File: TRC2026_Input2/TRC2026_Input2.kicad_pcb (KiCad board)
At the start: 2 copper layers, 144 x 63.3 mm, 26 parts, among them J1 ジョイスティック, J2 Conn_01x06_Pin, J3 Conn_01x05_Pin, J4 1F接続, J5 Conn_01x05_Pin, J6 Conn_01x05_Pin, SW1 SW_Push, SW2 SW_Push, SW3 SW_Push, SW4 SW_Push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

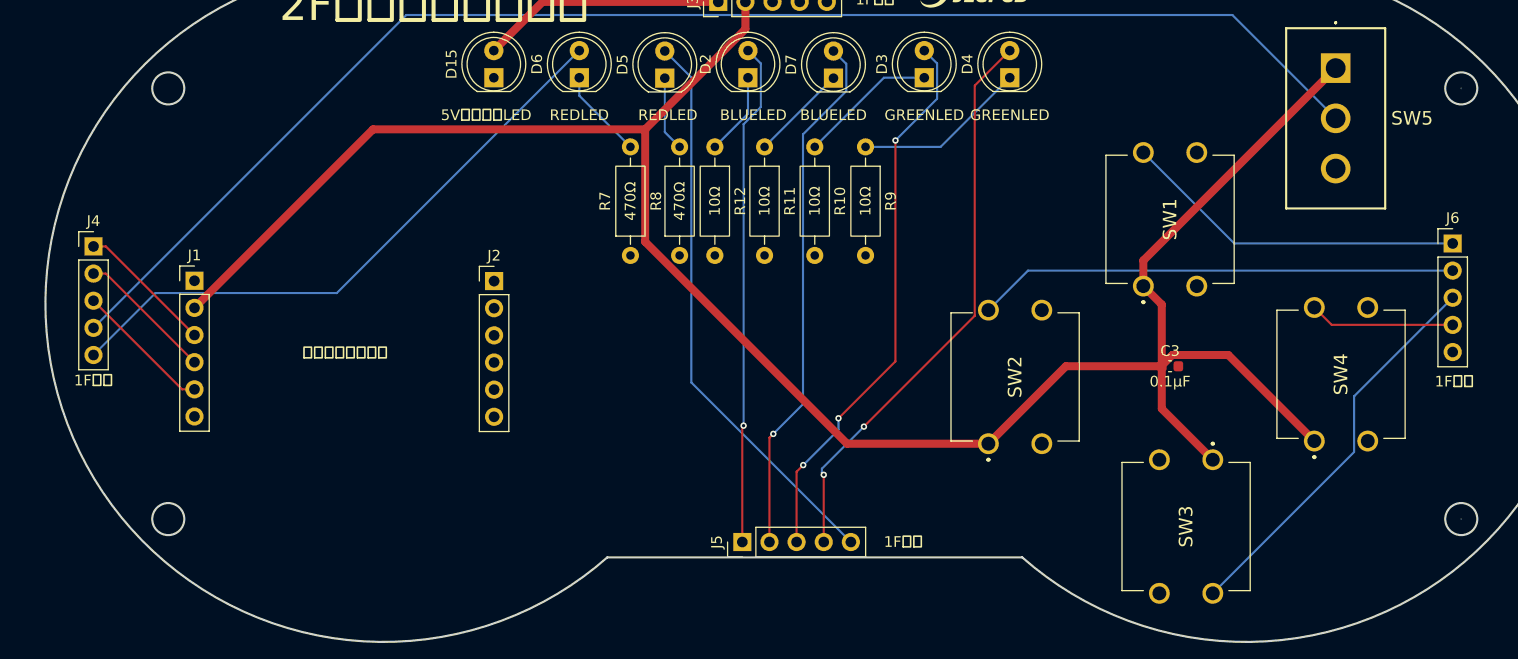
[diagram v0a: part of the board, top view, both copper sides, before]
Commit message: プルダウン抵抗とフットプリントを修正しました
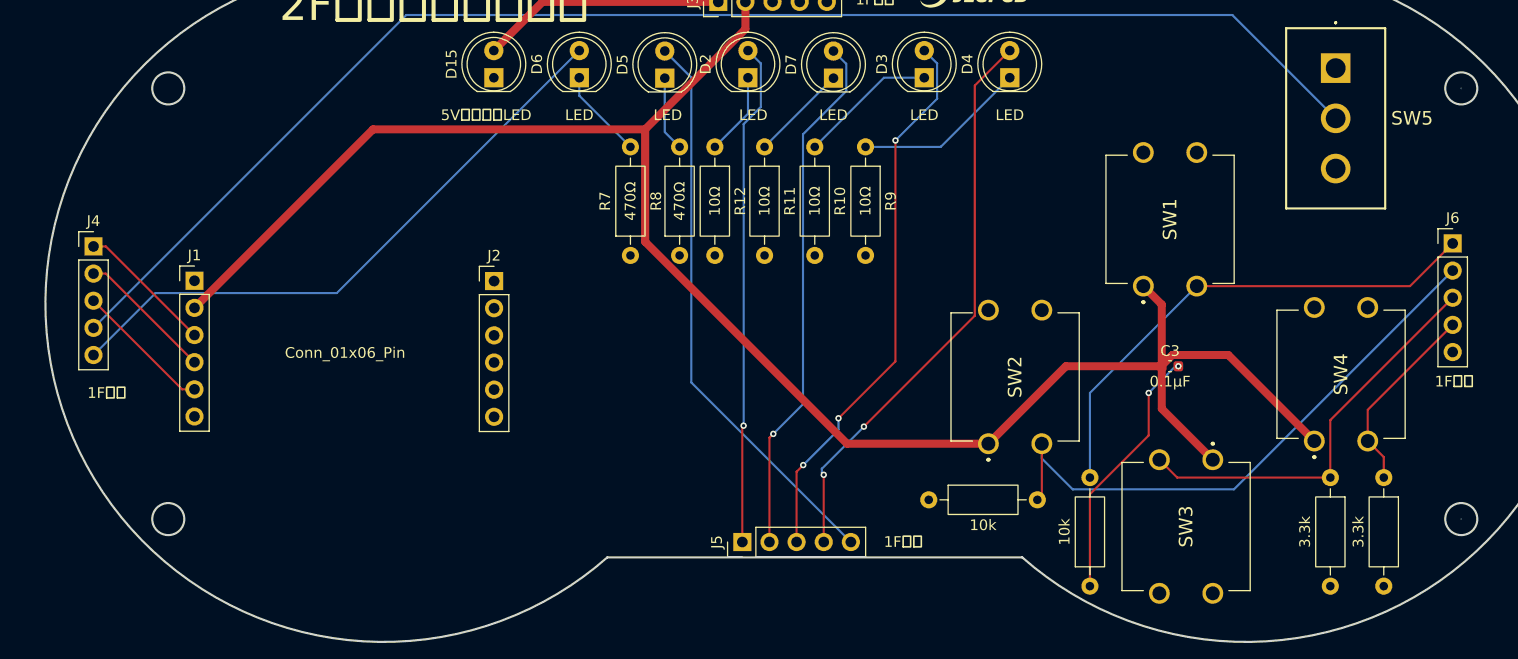
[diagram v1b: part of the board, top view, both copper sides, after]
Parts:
- added 10k: 3.3k, Resistor_THT:R_Axial_DIN0207_L6.3mm_D2.5mm_P10.16mm_Horizontal, F.Cu at (178.0, 118.6)
- added R2: 3.3k, Resistor_THT:R_Axial_DIN0207_L6.3mm_D2.5mm_P10.16mm_Horizontal, F.Cu at (200.5, 108.4)
- added R3: 3.3k, Resistor_THT:R_Axial_DIN0207_L6.3mm_D2.5mm_P10.16mm_Horizontal, F.Cu at (205.5, 108.4)
- added R4: 10k, Resistor_THT:R_Axial_DIN0207_L6.3mm_D2.5mm_P10.16mm_Horizontal, F.Cu at (162.9, 110.5)
- D2, D7: value BLUELED -> LED
- D3, D4: value GREENLED -> LED
- D5, D6: value REDLED -> LED
- J1: value ジョイスティック -> Conn_01x06_Pin
- J4: value 1F接続 -> Conn_01x05_Pin
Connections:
- SW5 pad 1: +3.3V -> unconnected-(SW5-A-Pad1)
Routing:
- net +3.3V: track 199.5 -> 171.6 mm
- net GND: track 0.00 -> 24.2 mm, vias 0 -> 2
- net GP2: track 32.5 -> 47.7 mm
- net GP3: track 45.0 -> 54.9 mm
- net GP5: track 13.6 -> 18.2 mm
- net GP4: track 37.0 -> 38.3 mm
